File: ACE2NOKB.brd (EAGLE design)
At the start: 160 x 100 mm, 100 parts, among them IC1 7805T, IC2 74367N, Q1 2N3904, Q2 2N3904, Q3 BC237, X1 6.556MHz, X8 2516-

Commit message: Update after faults pointed out by Claudius. Decoding address from 8k-16k changed. Transistor changed. Minor changed to take advantage of Hex Invert chip and remove cludged inverts.
Signed-off-by: John Bradley <flypie@rocketmail.com>
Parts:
- moved R21 262.7 mm to (129.5, 82.5)
- moved R6 261.9 mm to (151.1, 8.89)
- moved Z19 261.7 mm to (152.4, 43.2), turned to 270 degrees
- moved R20 257.1 mm to (129.5, 78.7)
- moved R5 253.8 mm to (152.4, 5.08)
- moved R19 251.6 mm to (129.5, 74.9)
- moved R18 246.2 mm to (129.5, 71.1)
- moved SV3 242.2 mm to (154.9, 102.9)
- moved Z24 241.0 mm to (124.5, 15.2), turned to 270 degrees
- moved R17 240.9 mm to (129.5, 67.3)
- moved R16 235.7 mm to (129.5, 63.5)
- moved Z28 234.1 mm to (111.8, 12.7), turned to 270 degrees
- moved Z23 233.0 mm to (138.4, 21.6), turned to 270 degrees
- moved RN2 231.1 mm to (109.2, 33.0)
- moved R15 230.6 mm to (129.5, 59.7)
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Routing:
- net GND: track 0.00 -> 855.6 mm, vias 0 -> 7
- net VCC: track 0.00 -> 855.5 mm, vias 0 -> 7
- net CNT8: track 0.00 -> 347.6 mm, vias 0 -> 5
- net N$8: track 0.00 -> 309.1 mm, vias 0 -> 7
- net N$3: track 0.00 -> 287.7 mm, vias 0 -> 9
- net ADDRESS10: track 0.00 -> 280.6 mm, vias 0 -> 6
- net CNT5: track 0.00 -> 278.9 mm, vias 0 -> 9
- net ADDRESS9: track 0.00 -> 264.0 mm, vias 0 -> 9
- net ADDRESS0: track 0.00 -> 260.6 mm, vias 0 -> 6
- net DATA0: track 0.00 -> 255.4 mm, vias 0 -> 9
- net ADDRESS7: track 0.00 -> 252.1 mm, vias 0 -> 7
- net CNT0: track 0.00 -> 249.5 mm, vias 0 -> 3
- net N$86: track 0.00 -> 248.8 mm, vias 0 -> 10
- net /VHOLD: track 0.00 -> 238.6 mm, vias 0 -> 11
- net ADDRESS8: track 0.00 -> 231.7 mm, vias 0 -> 7
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
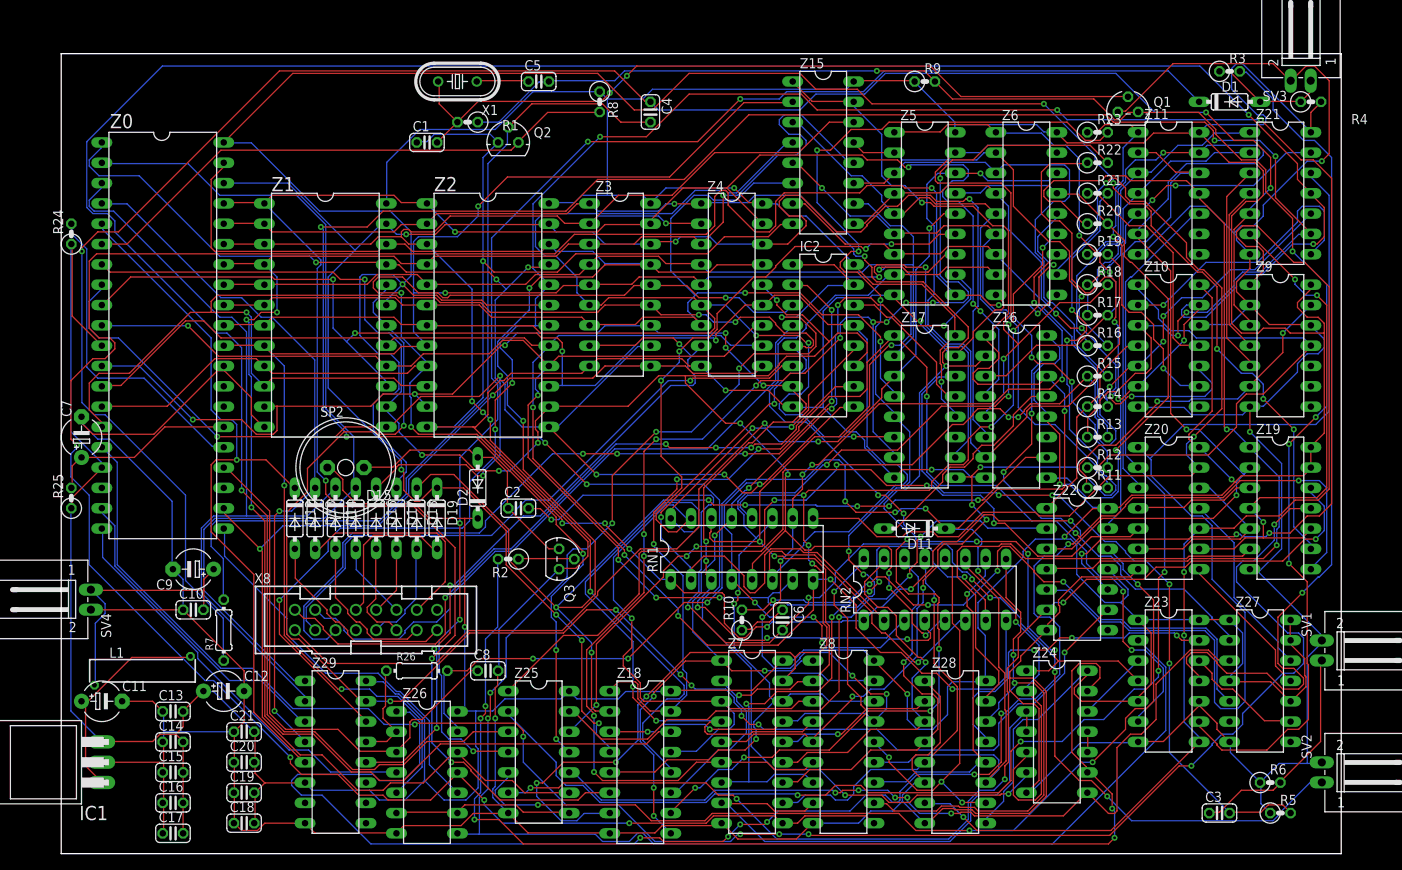
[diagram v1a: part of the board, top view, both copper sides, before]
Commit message: Sent test of ACE2NOKB for PCB manufacture as risk reduction execise to show schematic works.
Signed-off-by: John Bradley <flypie@rocketmail.com>
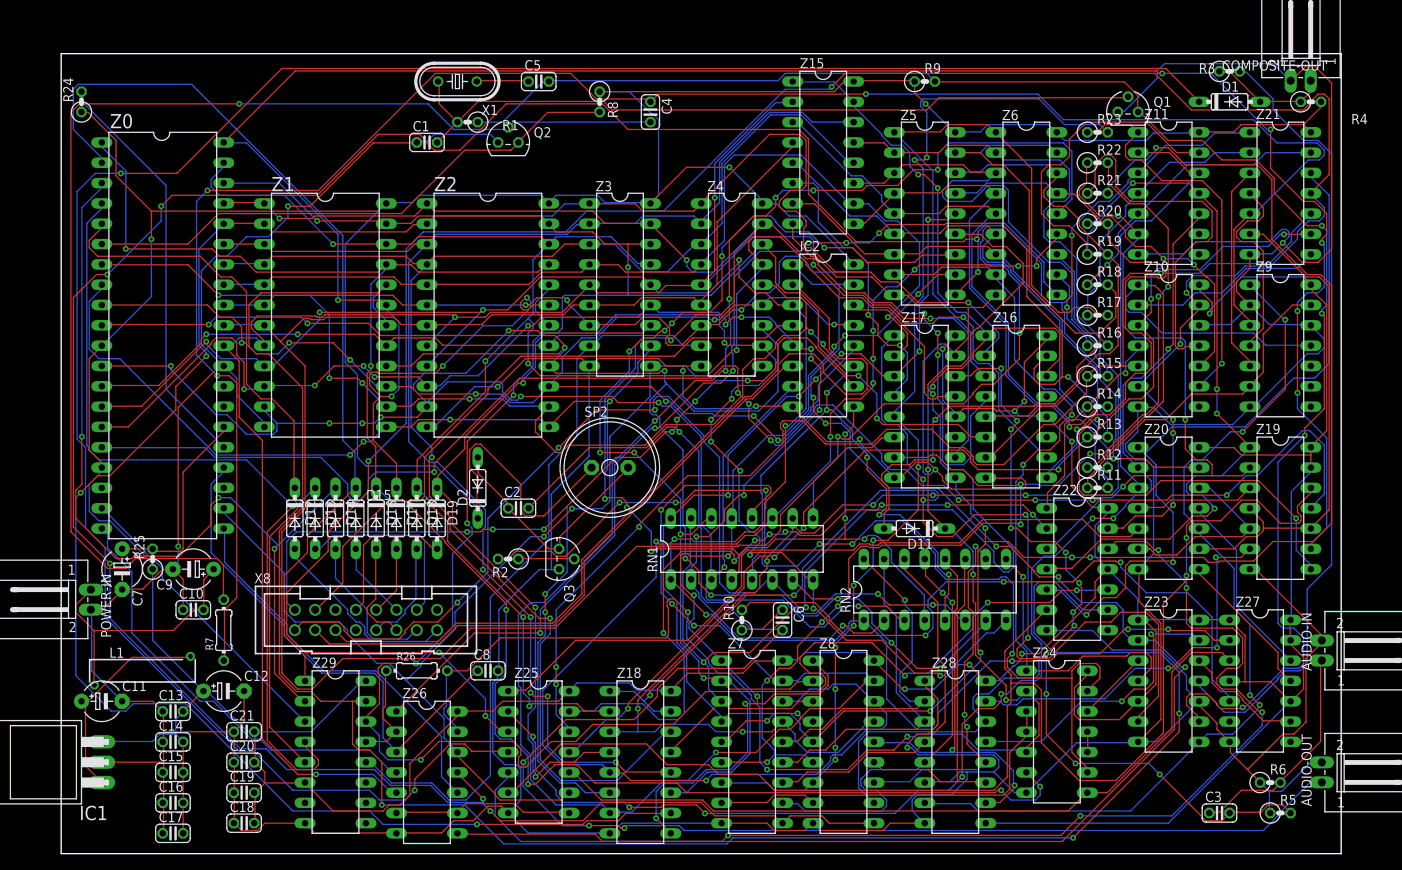
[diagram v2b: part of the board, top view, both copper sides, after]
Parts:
- moved SP2 33.0 mm to (68.6, 48.3)
- moved C7 17.3 mm to (7.62, 35.6), turned to 270 degrees
- moved R24 16.6 mm to (2.54, 94.0)
- moved R25 12.7 mm to (11.4, 36.8)
- renumbered SV1 to AUDIO-IN, SV2 to AUDIO-OUT, SV3 to COMPOSITE-OUT, SV4 to POWER-IN
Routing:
- net CNT5: track 278.9 -> 135.1 mm, vias 9 -> 6
- net N$3: track 287.7 -> 189.0 mm, vias 9 -> 7
- net N$51: track 173.3 -> 267.0 mm, vias 5 -> 2
- net N$20: track 166.9 -> 254.2 mm, vias 9 -> 10
- net ADDRESS6: track 208.4 -> 279.0 mm, vias 8 -> 4
- net N$1: track 185.4 -> 255.0 mm, vias 8 -> 3
- net N$71: track 125.0 -> 183.5 mm
- net N$43: track 152.7 -> 204.7 mm, vias 7 -> 4
- net ADDRESS1: track 173.9 -> 225.2 mm, vias 3 -> 0
- net CNT8: track 347.6 -> 296.4 mm, vias 5 -> 9
- net N$26: track 107.0 -> 153.2 mm, vias 0 -> 1
- net DATA1: track 222.1 -> 176.3 mm, vias 5 -> 13
- net N$84: track 133.8 -> 173.3 mm, vias 7 -> 9
- net N$49: track 129.6 -> 90.2 mm, vias 0 -> 2
- net /VHOLD: track 238.6 -> 199.6 mm, vias 11 -> 9
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
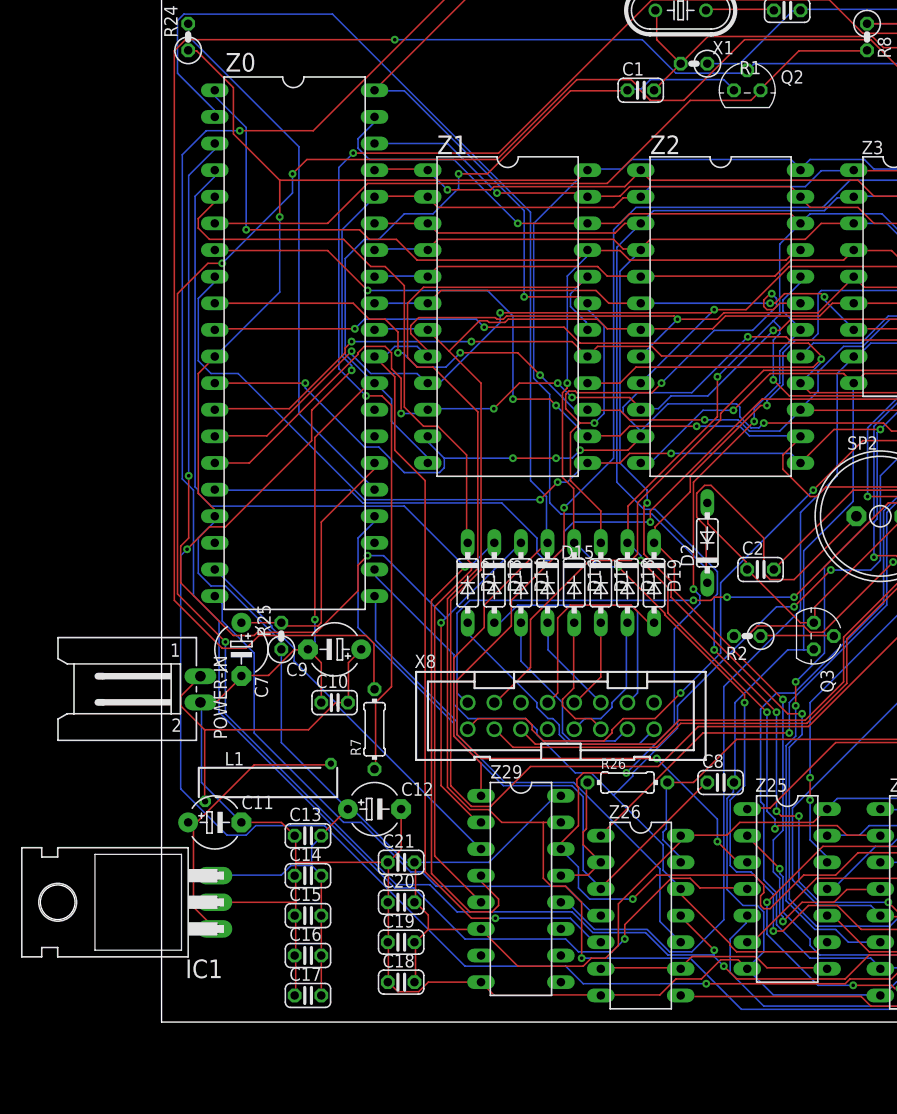
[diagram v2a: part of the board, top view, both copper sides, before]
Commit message: Fix transistor choice.
Signed-off-by: John Bradley <flypie@rocketmail.com>
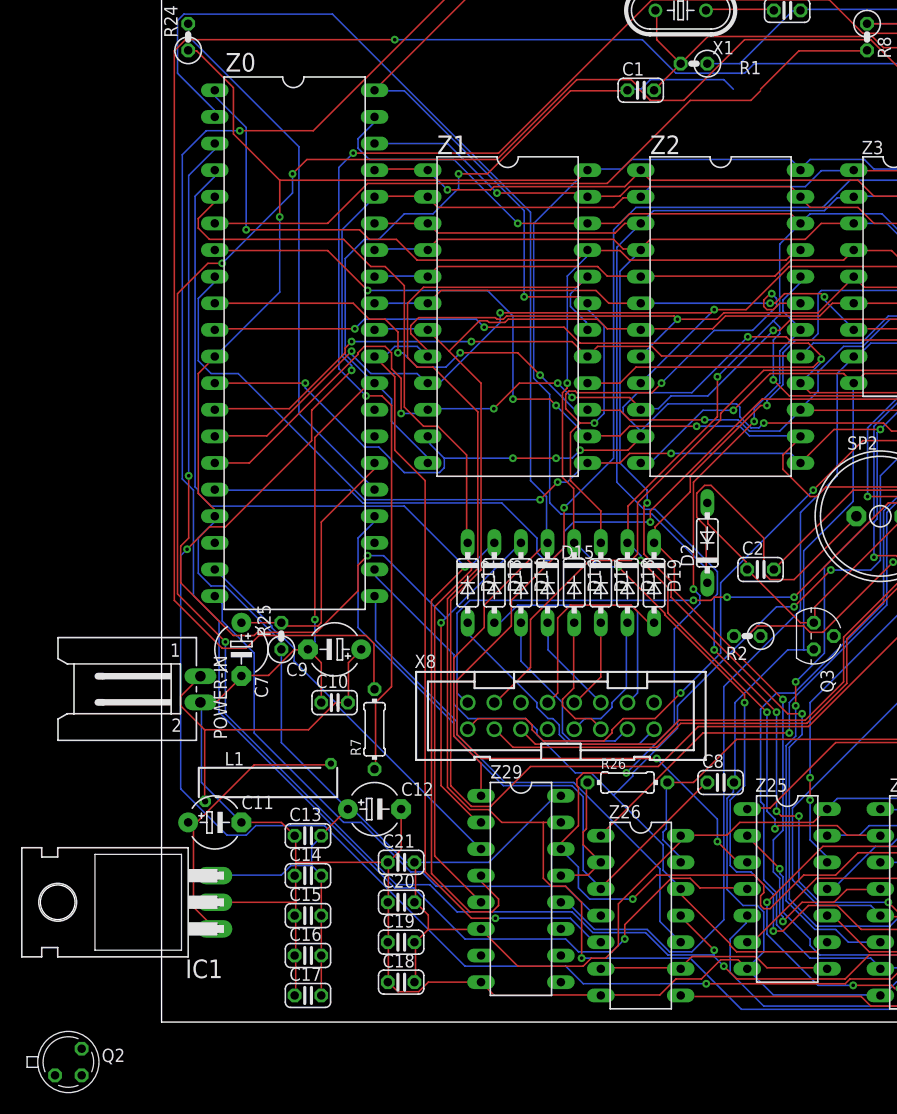
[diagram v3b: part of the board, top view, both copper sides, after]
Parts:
- Q2: value 2N3904 -> 2N2369; device transistor:TO92 -> transistor:TO18
- moved Q2 113.1 mm to (-8.89, -3.81)
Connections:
- net GND: now also Q2.1; no longer Q2.3
- net N$24: now also Q2.3; no longer Q2.1
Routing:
- net N$40: track 7.05 -> 0.00 mm
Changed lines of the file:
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@@
 <?xml version="1.0" encoding="utf-8"?>
 <!DOCTYPE eagle SYSTEM "eagle.dtd">
-<eagle version="9.4.1">
+<eagle version="9.4.2">
 <drawing>
 <settings>
@@
 <attribute name="VALUE" x="136.525" y="91.44" size="1.27" layer="27" ratio="10"/>
 </element>
-<element name="Q2" library="transistor" library_urn="urn:adsk.eagle:library:402" package="TO92" package3d_urn="urn:adsk.eagle:package:28523/2" value="2N3904" x="55.88" y="88.9" smashed="yes">
-<attribute name="NAME" x="59.055" y="89.535" size="1.27" layer="25" ratio="10"/>
-<attribute name="VALUE" x="59.055" y="87.63" size="1.27" layer="27" ratio="10"/>
-</element>
 <element name="Q3" library="transistor" library_urn="urn:adsk.eagle:library:402" package="TO92" package3d_urn="urn:adsk.eagle:package:28523/2" value="BC237" x="62.23" y="36.83" smashed="yes" rot="R270">
 <attribute name="NAME" x="62.865" y="33.655" size="1.27" layer="25" ratio="10" rot="R270"/>
@@
 <attribute name="VALUE" x="151.765" y="70.231" size="1.27" layer="27" ratio="10" rot="R270"/>
 </element>
+<element name="Q2" library="transistor" library_urn="urn:adsk.eagle:library:402" package="TO18" package3d_urn="urn:adsk.eagle:package:28526/2" value="2N2369" x="-8.89" y="-3.81" smashed="yes">
+<attribute name="NAME" x="-5.715" y="-3.81" size="1.27" layer="25" ratio="10"/>
+<attribute name="VALUE" x="-5.715" y="-5.715" size="1.27" layer="27" ratio="10"/>
+</element>
 </elements>
 <signals>
@@
 <contactref element="Z17" pad="15"/>
 <contactref element="Z28" pad="6"/>
-<contactref element="Q2" pad="3"/>
 <contactref element="C8" pad="2"/>
 <contactref element="C7" pad="-"/>
@@
 <wire x1="54.5592" y1="89.0016" x2="53.6448" y2="89.916" width="0.1524" layer="16"/>
 <wire x1="44.5008" y1="89.0016" x2="44.45" y2="88.9" width="0.1524" layer="16"/>
-<wire x1="54.5592" y1="89.0016" x2="54.61" y2="88.9" width="0.1524" layer="16"/>
 <wire x1="25.2984" y1="53.9496" x2="25.2984" y2="53.34" width="0.1524" layer="16"/>
 <wire x1="21.9456" y1="57.3024" x2="25.2984" y2="53.9496" width="0.1524" layer="16"/>
@@
 <via x="86.868" y="55.9308" extent="1-16" drill="0.35"/>
 <via x="77.724" y="60.3504" extent="1-16" drill="0.35"/>
+<contactref element="Q2" pad="1"/>
+<wire x1="-10.16" y1="-5.08" x2="5.08" y2="11.43" width="0" layer="19" extent="1-1"/>
 </signal>
 <signal name="ADDRESS0">
@@
 <contactref element="Z0" pad="6"/>
 <contactref element="R8" pad="2"/>
-<contactref element="Q2" pad="1"/>
 <wire x1="15.8496" y1="76.2" x2="5.1816" y2="76.2" width="0.1524" layer="1"/>
 <wire x1="19.6596" y1="80.01" x2="15.8496" y2="76.2" width="0.1524" layer="1"/>
@@
 <wire x1="57.15" y1="88.8492" x2="56.2356" y2="87.9348" width="0.1524" layer="1"/>
 <wire x1="5.1816" y1="76.2" x2="5.08" y2="76.2" width="0.1524" layer="1"/>
-<wire x1="57.15" y1="88.8492" x2="57.15" y2="88.9" width="0.1524" layer="1"/>
 <wire x1="60.8076" y1="92.6592" x2="67.2084" y2="92.6592" width="0.1524" layer="1"/>
 <wire x1="57.15" y1="89.0016" x2="60.8076" y2="92.6592" width="0.1524" layer="1"/>
 <wire x1="67.2084" y1="92.6592" x2="67.31" y2="92.71" width="0.1524" layer="1"/>
-<wire x1="57.15" y1="89.0016" x2="57.15" y2="88.9" width="0.1524" layer="1"/>
+<contactref element="Q2" pad="3"/>
+<wire x1="57.15" y1="88.8492" x2="57.15" y2="89.0016" width="0" layer="19" extent="1-1"/>
+<wire x1="-7.62" y1="-2.54" x2="5.08" y2="76.2" width="0" layer="19" extent="1-1"/>
 </signal>
 <signal name="N$26">
 <contactref element="R7" pad="2"/>
-<contactref element="Q2" pad="2"/>
 <contactref element="C4" pad="2"/>
 <wire x1="20.2692" y1="36.1188" x2="20.2692" y2="31.8516" width="0.1524" layer="1"/>
@@
 <wire x1="55.7784" y1="90.678" x2="55.626" y2="90.5256" width="0.1524" layer="16"/>
 <wire x1="20.2692" y1="31.8516" x2="20.32" y2="31.75" width="0.1524" layer="1"/>
-<wire x1="55.7784" y1="90.678" x2="55.88" y2="90.805" width="0.1524" layer="16"/>
 <wire x1="56.5404" y1="91.44" x2="73.6092" y2="91.44" width="0.1524" layer="16"/>
 <wire x1="55.9308" y1="90.8304" x2="56.5404" y2="91.44" width="0.1524" layer="16"/>
 <wire x1="73.6092" y1="91.44" x2="73.66" y2="91.44" width="0.1524" layer="16"/>
-<wire x1="55.9308" y1="90.8304" x2="55.88" y2="90.805" width="0.1524" layer="16"/>
 <via x="22.2504" y="93.726" extent="1-16" drill="0.35"/>
+<contactref element="Q2" pad="2"/>
+<wire x1="55.7784" y1="90.678" x2="55.9308" y2="90.8304" width="0" layer="19" extent="16-16"/>
+<wire x1="-7.62" y1="-5.08" x2="5.7912" y2="35.6616" width="0" layer="19" extent="1-1"/>
 </signal>
 <signal name="N$28">
@@
 <wire x1="134.5692" y1="24.0792" x2="134.62" y2="24.13" width="0.1524" layer="1"/>
 </signal>
-<signal name="N$40">
-<contactref element="R2" pad="1"/>
-<contactref element="Q3" pad="2"/>
-<wire x1="64.008" y1="36.8808" x2="57.15" y2="36.8808" width="0.1524" layer="1"/>
-<wire x1="57.15" y1="36.8808" x2="57.15" y2="36.83" width="0.1524" layer="1"/>
-<wire x1="64.008" y1="36.8808" x2="64.135" y2="36.83" width="0.1524" layer="1"/>
-</signal>
 <signal name="N$41">
 <contactref element="R10" pad="2"/>
@@
 <wire x1="36.8808" y1="30.48" x2="36.83" y2="30.48" width="0.1524" layer="1"/>
 </signal>
+<signal name="N$40">
+<contactref element="R2" pad="1"/>
+<contactref element="Q3" pad="2"/>
+<wire x1="57.15" y1="36.83" x2="64.135" y2="36.83" width="0" layer="19" extent="1-1"/>
+</signal>
 </signals>
